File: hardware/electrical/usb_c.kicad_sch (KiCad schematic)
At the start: 4 parts, among them U1 USBLC6-2SC6

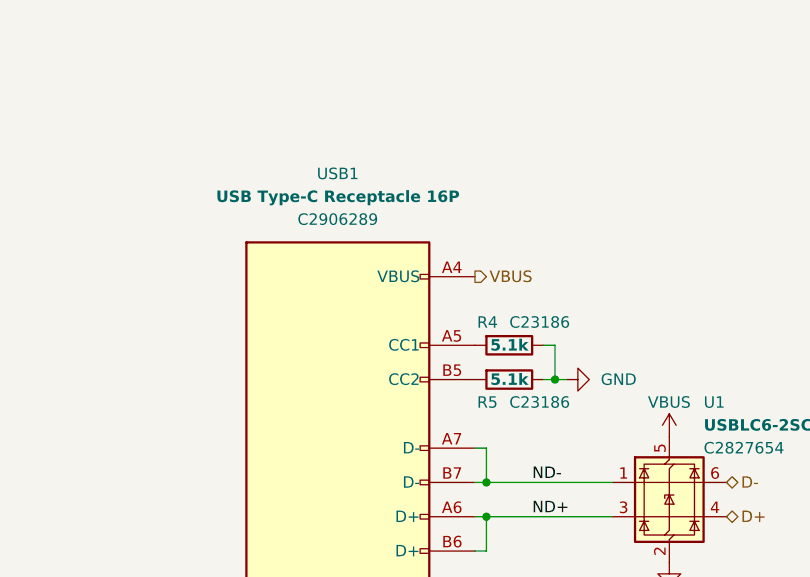
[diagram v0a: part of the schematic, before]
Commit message: Update schematic to include regulators and switches, update render
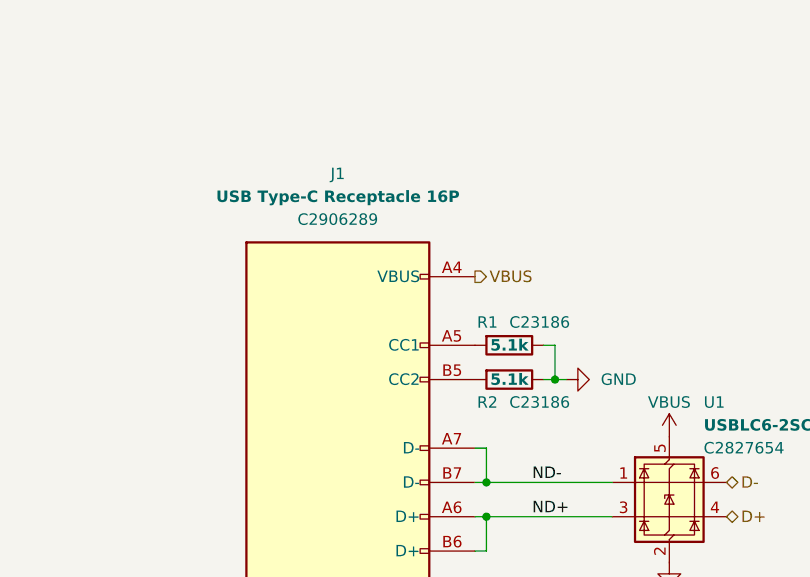
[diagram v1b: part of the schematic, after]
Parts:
- renumbered USB1 to J1, R4 to R1, R5 to R2
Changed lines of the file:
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@@
 	(title_block
 		(title "HexTrack PCB")
-		(date "2025-01-09")
-		(rev "v0.0.1")
+		(date "2025-02-01")
+		(rev "v0.0.2")
 		(company "TMShader")
 		(comment 9 "HexTrack")
@@
 		(on_board yes)
 		(dnp no)
-		(property "Reference" "R4"
+		(property "Reference" "R1"
 			(at 146.05 88.9 90)
 			(effects
@@
 			(project "hextrack"
 				(path "/e03ae3c5-ddb7-48ac-a408-9dcc58a57689/9836e963-ec32-4c01-99da-5c973017755a/b85208ae-6025-47c1-ac11-02f6f1e1bd30"
-					(reference "R4")
+					(reference "R1")
 					(unit 1)
 				)
@@
 		(on_board yes)
 		(dnp no)
-		(property "Reference" "#PWR016"
+		(property "Reference" "#PWR07"
 			(at 165.1 121.92 0)
 			(effects
@@
 			(project "hextrack"
 				(path "/e03ae3c5-ddb7-48ac-a408-9dcc58a57689/9836e963-ec32-4c01-99da-5c973017755a/b85208ae-6025-47c1-ac11-02f6f1e1bd30"
-					(reference "#PWR016")
+					(reference "#PWR07")
 					(unit 1)
 				)
@@
 		(on_board yes)
 		(dnp no)
-		(property "Reference" "#PWR017"
+		(property "Reference" "#PWR06"
 			(at 165.1 105.41 0)
 			(effects
@@
 			(project ""
 				(path "/e03ae3c5-ddb7-48ac-a408-9dcc58a57689/9836e963-ec32-4c01-99da-5c973017755a/b85208ae-6025-47c1-ac11-02f6f1e1bd30"
-					(reference "#PWR017")
+					(reference "#PWR06")
 					(unit 1)
 				)
@@
 		(on_board yes)
 		(dnp no)
-		(property "Reference" "USB1"
+		(property "Reference" "J1"
 			(at 128.27 72.39 0)
 			(effects
@@
 			(project ""
 				(path "/e03ae3c5-ddb7-48ac-a408-9dcc58a57689/9836e963-ec32-4c01-99da-5c973017755a/b85208ae-6025-47c1-ac11-02f6f1e1bd30"
-					(reference "USB1")
+					(reference "J1")
 					(unit 1)
 				)
@@
 		(on_board yes)
 		(dnp no)
-		(property "Reference" "R5"
+		(property "Reference" "R2"
 			(at 146.05 97.79 90)
 			(effects
@@
 			(project "hextrack"
 				(path "/e03ae3c5-ddb7-48ac-a408-9dcc58a57689/9836e963-ec32-4c01-99da-5c973017755a/b85208ae-6025-47c1-ac11-02f6f1e1bd30"
-					(reference "R5")
+					(reference "R2")
 					(unit 1)
 				)
@@
 		(on_board yes)
 		(dnp no)
-		(property "Reference" "#PWR014"
+		(property "Reference" "#PWR08"
 			(at 128.27 140.97 0)
 			(effects
@@
 			(project "hextrack"
 				(path "/e03ae3c5-ddb7-48ac-a408-9dcc58a57689/9836e963-ec32-4c01-99da-5c973017755a/b85208ae-6025-47c1-ac11-02f6f1e1bd30"
-					(reference "#PWR014")
+					(reference "#PWR08")
 					(unit 1)
 				)
@@
 		(on_board yes)
 		(dnp no)
-		(property "Reference" "#PWR015"
+		(property "Reference" "#PWR05"
 			(at 160.02 95.25 0)
 			(effects
@@
 			(project "hextrack"
 				(path "/e03ae3c5-ddb7-48ac-a408-9dcc58a57689/9836e963-ec32-4c01-99da-5c973017755a/b85208ae-6025-47c1-ac11-02f6f1e1bd30"
-					(reference "#PWR015")
+					(reference "#PWR05")
 					(unit 1)
 				)
